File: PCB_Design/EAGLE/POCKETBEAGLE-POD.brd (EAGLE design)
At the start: 100.3 x 58.4 mm, 29 parts, among them CN1 1, U1 POCKETBEAGLE, X1 STEREOJACK

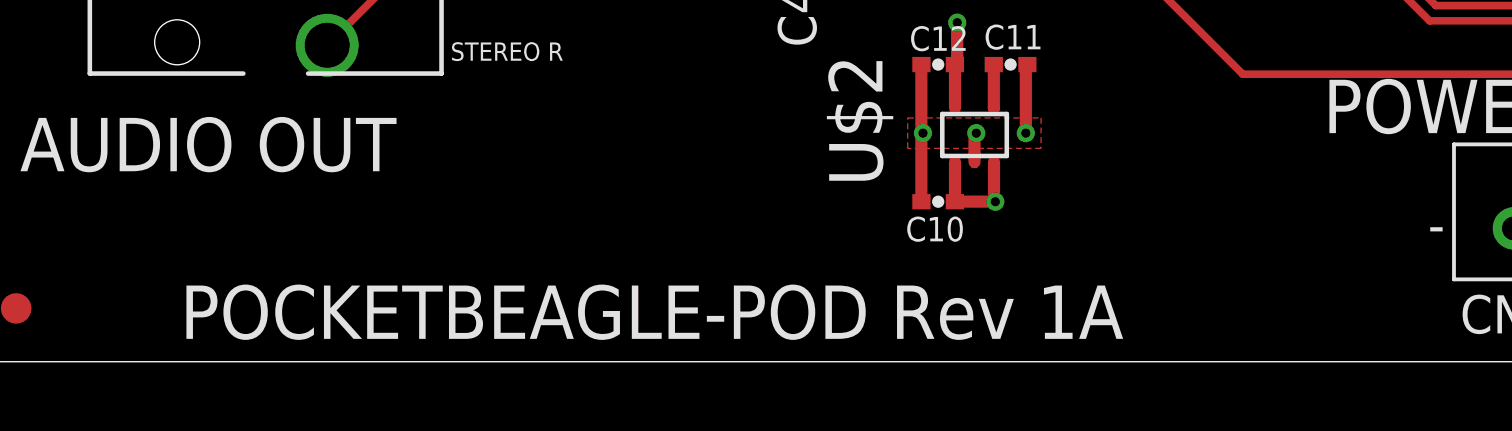
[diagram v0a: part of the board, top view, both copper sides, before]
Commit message: Documentation Fixes
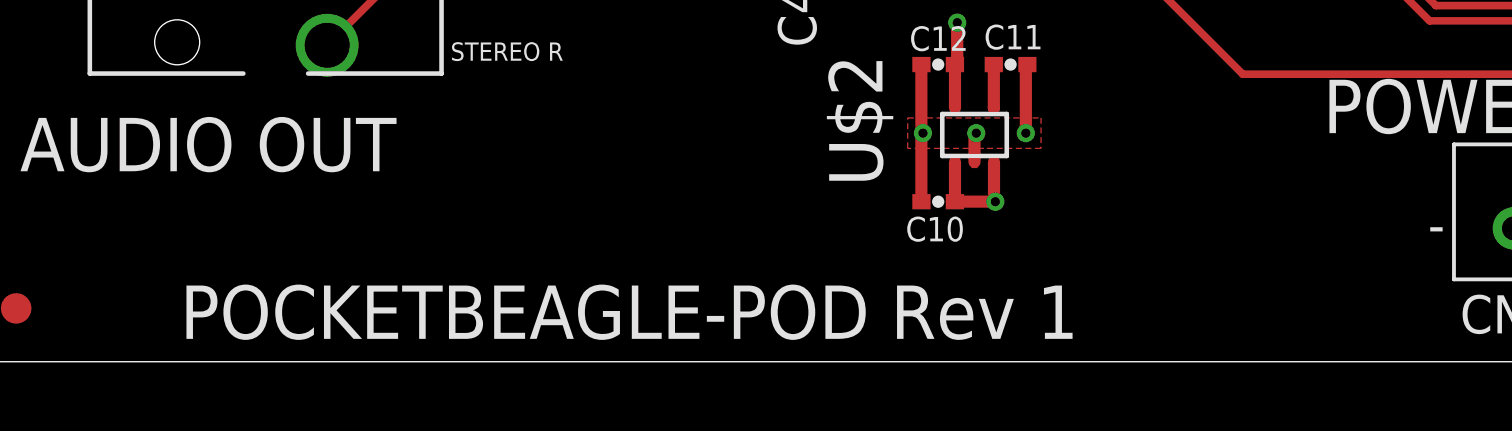
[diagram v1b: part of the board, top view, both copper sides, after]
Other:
- board text added: "POCKETBEAGLE-POD Rev 1"
- board text removed: "POCKETBEAGLE-POD Rev 1A"
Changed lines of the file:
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@@
 <text x="2.413" y="6.35" size="1.778" layer="21">AUDIO OUT</text>
 <text x="82.423" y="20.32" size="1.778" layer="21" rot="R90">POCKETBEAGLE</text>
-<text x="7.747" y="0.762" size="1.778" layer="21">POCKETBEAGLE-POD Rev 1A</text>
+<text x="7.747" y="0.762" size="1.778" layer="21">POCKETBEAGLE-POD Rev 1</text>
 <text x="26.162" y="29.464" size="0.6096" layer="21" rot="R90">P8 GND</text>
 <text x="23.622" y="29.464" size="0.6096" layer="21" rot="R90">P7 3.3V</text>
